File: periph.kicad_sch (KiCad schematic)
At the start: 37 parts, among them J11 Button, J12 Load, J7 USB_B_MINI, J8 Magnet, J9 iButton, Q1 IRF740, Q2 BCX56, Q3 AO3400A, U4 CH340N, U5 PC817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

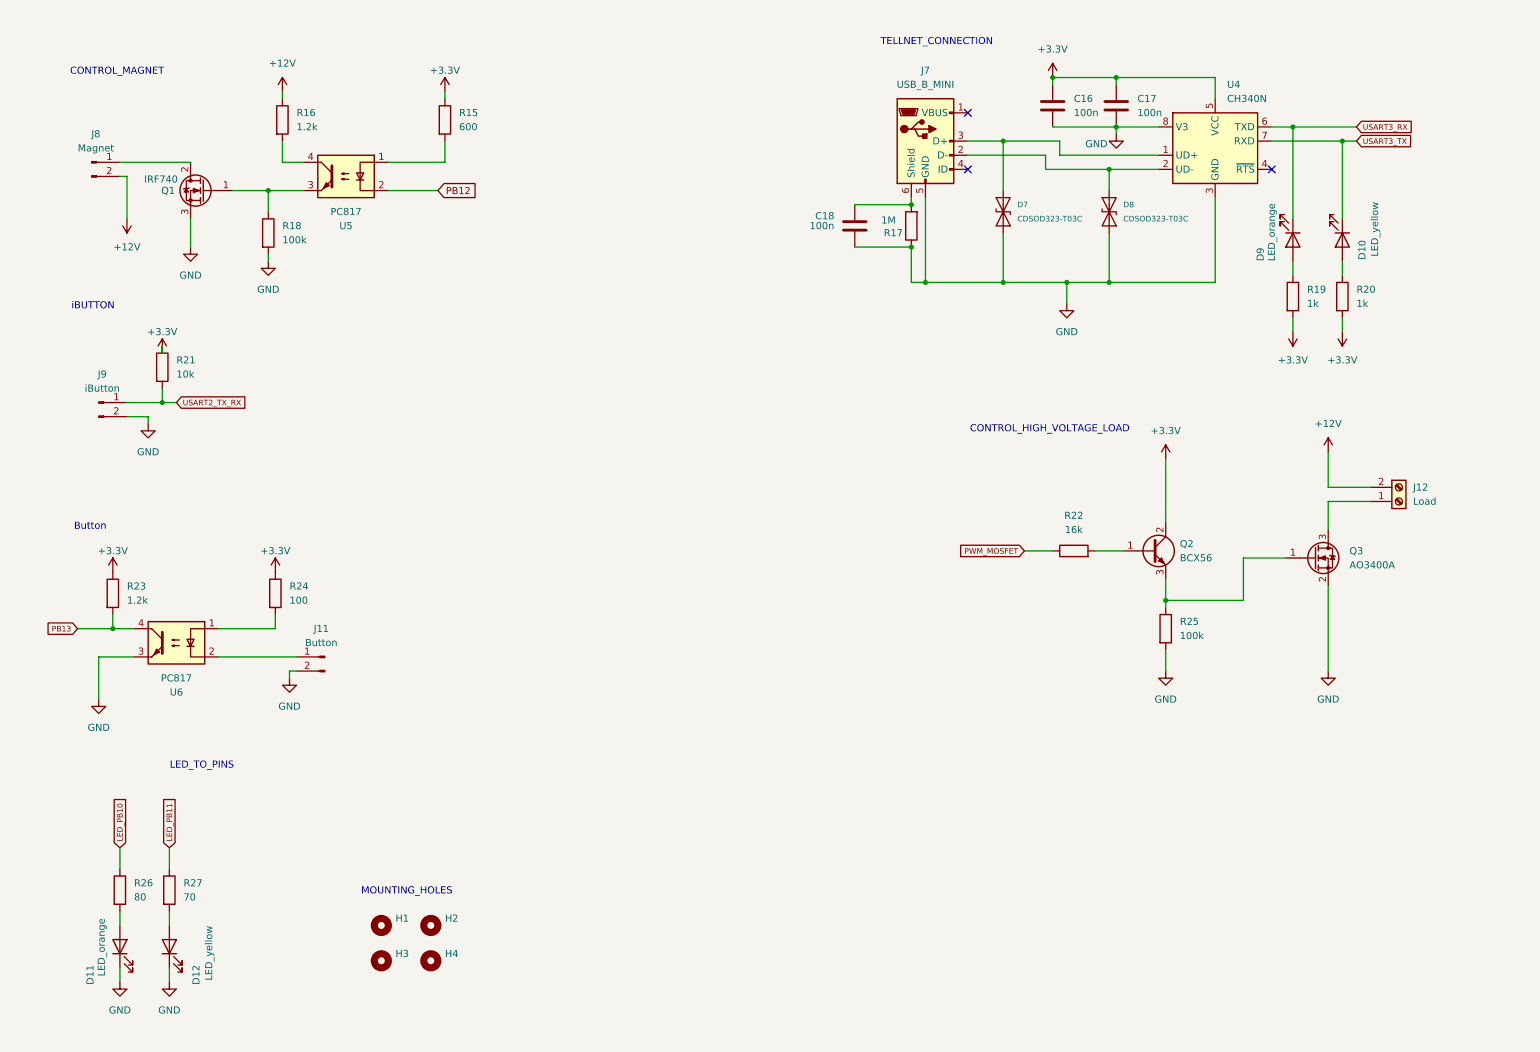
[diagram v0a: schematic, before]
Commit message: Some rearrangements have been made in schematics
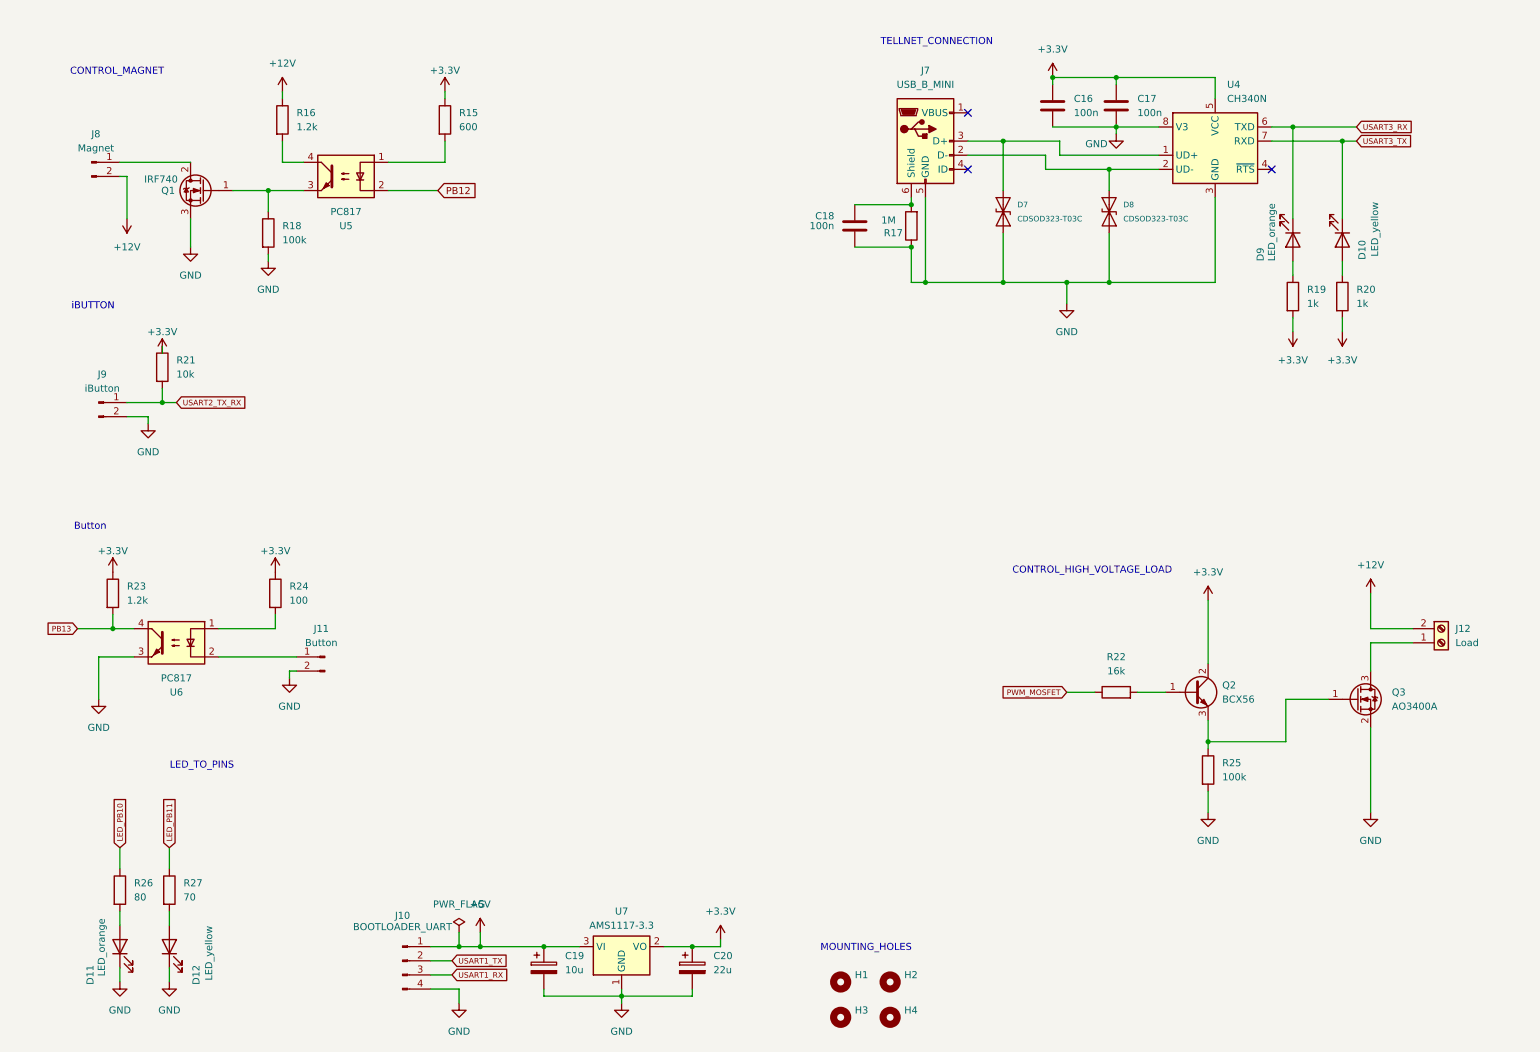
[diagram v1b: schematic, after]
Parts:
- added C19: 10u, Capacitor_Tantalum_SMD:CP_EIA-3216-12_Kemet-S_HandSolder, symbol Device:C_Polarized
- added C20: 22u, Capacitor_Tantalum_SMD:CP_EIA-3216-12_Kemet-S_HandSolder, symbol Device:C_Polarized
- added J10: BOOTLOADER_UART, Connector:NS-Tech_Grove_1x04_P2mm_Vertical, symbol Connector:Conn_01x04_Pin
- added U7: AMS1117-3.3, Package_TO_SOT_SMD:SOT-223-3_TabPin2, symbol Regulator_Linear:AMS1117-3.3
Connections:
- net +3.3V: now also C20.1, U7.2 (VO)
- net GND: now also C19.2, C20.2, J10.4 (Pin_4), U7.1 (GND)
- new net +5V: C19.1, J10.1 (Pin_1), U7.3 (VI)
- new net USART1_RX: J10.3 (Pin_3)
- new net USART1_TX: J10.2 (Pin_2)
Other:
- moved on the sheet: H1, H2, H3, H4, J12, Q2, Q3, R22, R25

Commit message: Frames in schematics has been added. Types of mounting holes has been replaced
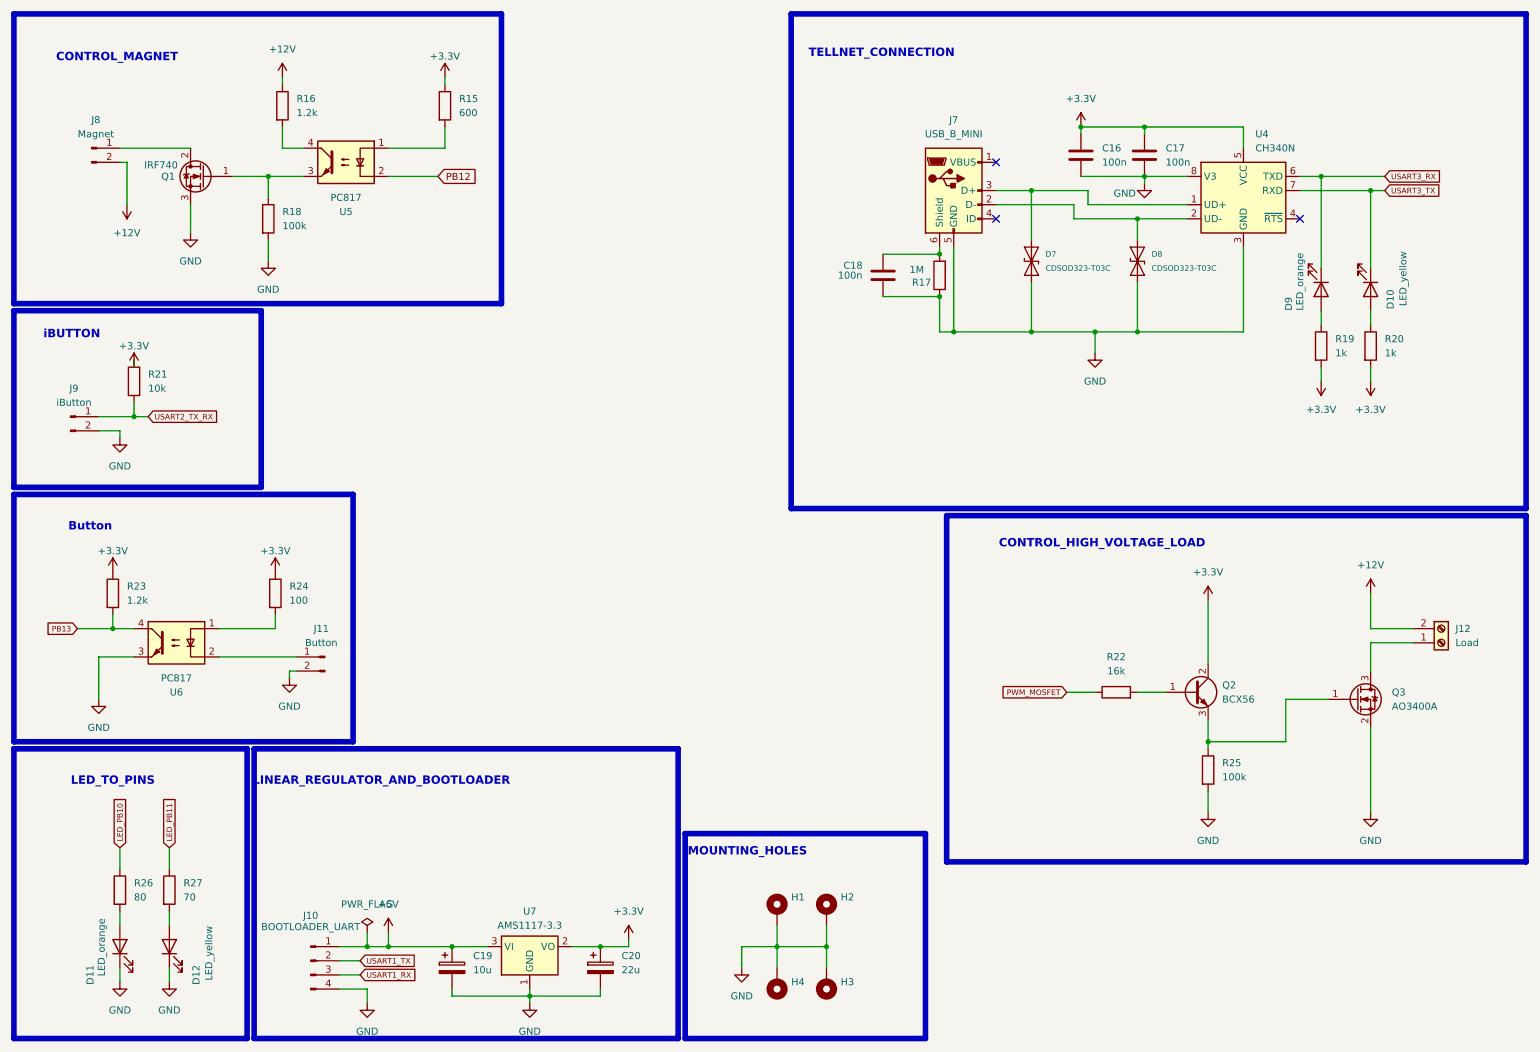
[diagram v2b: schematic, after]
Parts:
- removed H1, H2, H3, H4: MountingHole, MountingHole:MountingHole_2.7mm_M2.5_ISO14580, symbol Mechanical:MountingHole
- added H1, H2, H3, H4: MountingHole_Pad, MountingHole:MountingHole_3.2mm_M3_Pad_Via, symbol Mechanical:MountingHole_Pad
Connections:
- net GND: now also H1.1, H2.1, H3.1, H4.1
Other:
- note added: "LINEAR_REGULATOR_AND_BOOTLOADER"
- moved on the sheet: C16, C17, C18, C19, C20, D10, D7, D8, D9, J10, J7, J8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

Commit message: Comments have been added to the schemas
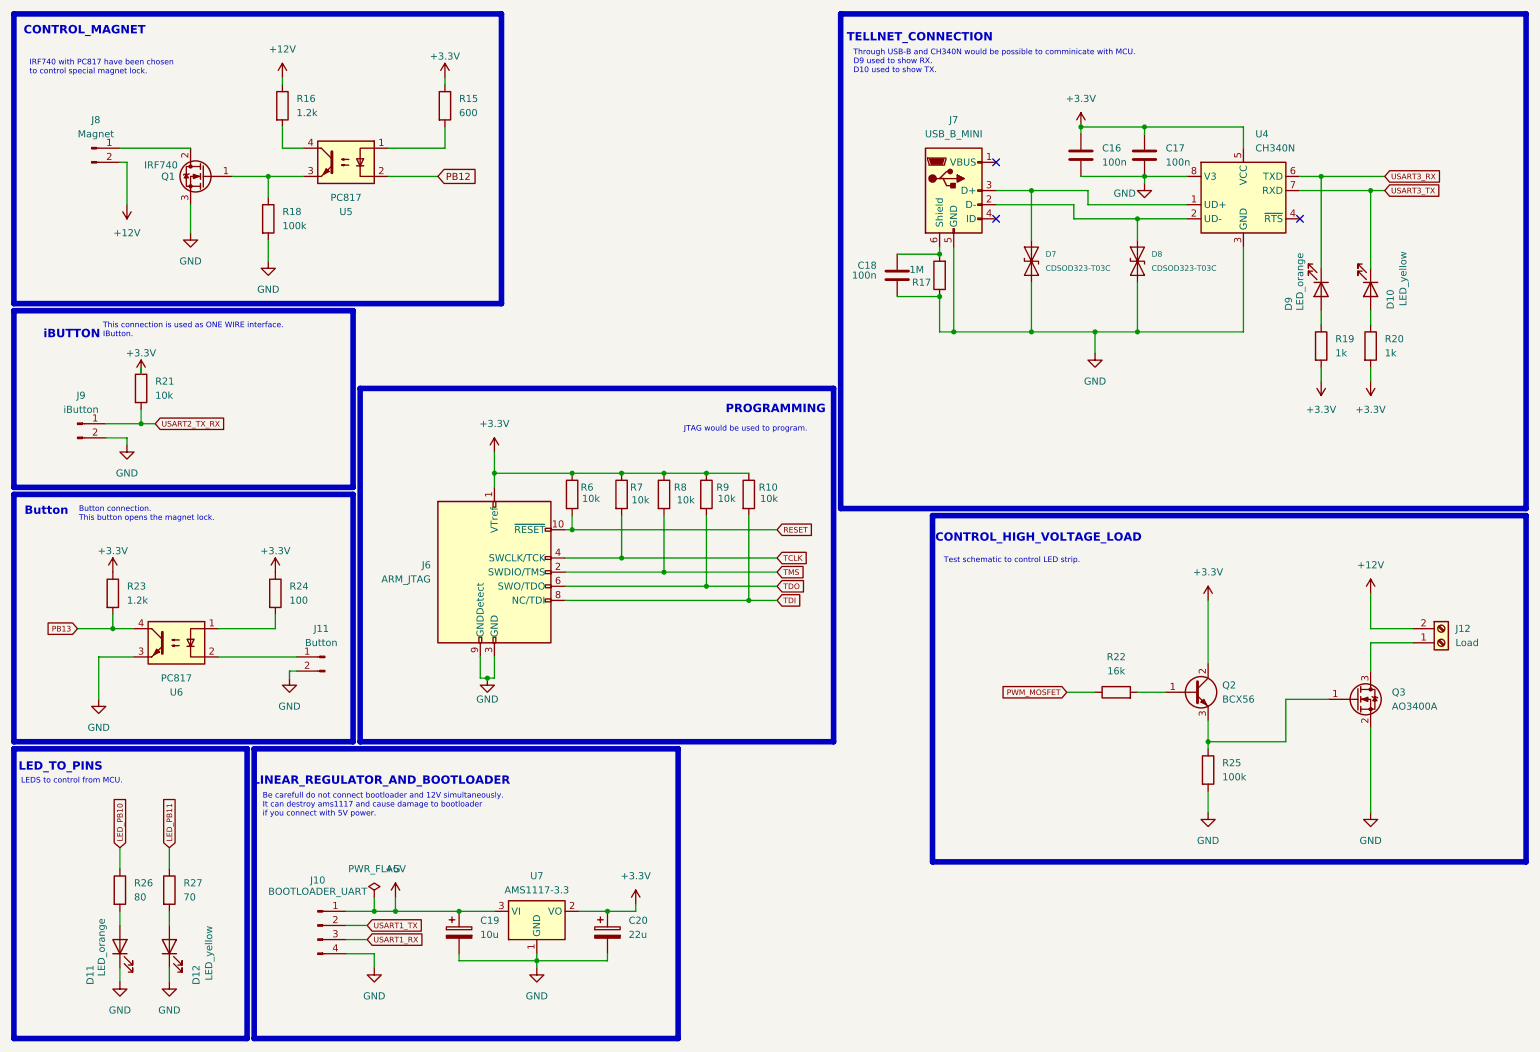
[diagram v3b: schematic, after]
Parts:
- removed H1, H2, H3, H4: MountingHole_Pad, MountingHole:MountingHole_3.2mm_M3_Pad_Via, symbol Mechanical:MountingHole_Pad
- added J6: ARM_JTAG, Connector_PinHeader_1.27mm:PinHeader_2x05_P1.27mm_Vertical, symbol Connector:Conn_ARM_JTAG_SWD_10
- added R10, R6, R7, R8, R9: 10k, Resistor_SMD:R_1206_3216Metric_Pad1.30x1.75mm_HandSolder, symbol Device:R
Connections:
- net +3.3V: now also J6.1 (VTref), R10.1, R6.1, R7.1, R8.1, R9.1
- net GND: now also J6.3 (GND), J6.5 (GND), J6.9 (GNDDetect)
- new net RESET: J6.10 (~{RESET}), R6.2
- new net TCLK: J6.4 (SWCLK/TCK), R7.2
- new net TDI: J6.8 (NC/TDI), R10.2
- new net TDO: J6.6 (SWO/TDO), R9.2
- new net TMS: J6.2 (SWDIO/TMS), R8.2
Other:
- note added: "Be carefull do not connect bootloader and 12V simultaneously. It can destroy ams1117 and cause damage to bootloader if you connect with 5V power."
- note added: "Button connection. This button opens the magnet lock."
- note added: "IRF740 with PC817 have been chosen to control special magnet lock."
- note added: "JTAG would be used to program."
- note added: "LEDS to control from MCU."
- note added: "PROGRAMMING"
- note added: "Test schematic to control LED strip."
- note added: "This connection is used as ONE WIRE interface. IButton."
- note added: "Through USB-B and CH340N would be possible to comminicate with MCU. D9 used to show RX. D10 used to show TX."
- note removed: "MOUNTING_HOLES"
- moved on the sheet: C18, C19, C20, J10, J9, R21, U7

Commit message: Footprints of bootloaders and boots have been changed also has been cahnged ADC pin header, reset LED have been added, and diode for switch
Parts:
- J10: footprint Connector:NS-Tech_Grove_1x04_P2mm_Vertical -> Connector_PinHeader_2.54mm:PinHeader_1x04_P2.54mm_Vertical
- J6: footprint Connector_PinHeader_1.27mm:PinHeader_2x05_P1.27mm_Vertical -> Connector_PinHeader_2.54mm:PinHeader_2x05_P2.54mm_Vertical
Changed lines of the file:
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@@
 			)
 		)
-		(property "Footprint" "Connector:NS-Tech_Grove_1x04_P2mm_Vertical"
+		(property "Footprint" "Connector_PinHeader_2.54mm:PinHeader_1x04_P2.54mm_Vertical"
 			(at 67.31 176.53 0)
 			(effects
@@
 			)
 		)
-		(property "Footprint" "Connector_PinHeader_1.27mm:PinHeader_2x05_P1.27mm_Vertical"
+		(property "Footprint" "Connector_PinHeader_2.54mm:PinHeader_2x05_P2.54mm_Vertical"
 			(at 99.06 113.03 0)
 			(effects
